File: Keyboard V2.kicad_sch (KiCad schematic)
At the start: 247 parts, among them J0 Conn_01x06_Pin, J1 Conn_01x05_Pin, J2 USB_C_Receptacle_USB2.0_16P, P1 SW_Push, SW1 ESC, SW10 F9, SW11 F10, SW12 F11, SW13 F12, SW14 PrntScrn, SW15 Til, SW16 1, SW17 2, SW18 3, SW19 4, SW2 F1, SW20 5, SW21 6, SW22 7, SW23 8, SW24 RotaryEncoder_Switch, SW25 9, SW26 0, SW27 Min, SW28 Plus, SW29 Bs, SW3 F2, SW30 Del, SW31 Tab, SW32 Q, SW33 W, SW34 E, SW35 R, SW36 T, SW37 Y, SW38 U, SW39 I, SW4 F3, SW40 O, SW41 P, SW42 LBrck, SW43 RBrck, SW44 BSlsh, SW45 Home, SW46 Caps, SW47 A, SW48 S, SW49 D, SW5 F4, SW50 F, SW51 G, SW52 H, SW53 J, SW54 K, SW55 L, SW56 Semi, SW57 Quot, SW58 Enter, SW59 End, SW6 F5, SW60 LShft, SW61 Z, SW62 X, SW63 C, SW64 V, SW65 B, SW66 N, SW67 M, SW68 Comma, SW69 Prd, SW7 F6, SW70 Slash, SW71 RShft, SW72 Up, SW73 LCtrl, SW74 Supr, SW75 Alt, SW76 Space, SW77 RAlt, SW78 Fn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

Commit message: finish esp32-31 version
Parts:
- removed C0: 5uF, symbol Device:C
- removed C109, C120: 1uF, Capacitor_SMD:C_0402_1005Metric, symbol Device:C
- removed C111, C96, C97: 2.2uF, Capacitor_SMD:C_0402_1005Metric, symbol Device:C
- removed C112, C113, C114, C117, C92, C93, C94, C95, C98: 100nF, Capacitor_SMD:C_0402_1005Metric, symbol Device:C
- removed C78, C89: 10uF, Capacitor_SMD:C_0805_2012Metric, symbol Device:C
- removed C88: 100nF, Capacitor_SMD:C_0603_1608Metric, symbol Device:C
- removed C90, C91: 30pF, Capacitor_SMD:C_0402_1005Metric, symbol Device:C
- removed FB1: FerriteBead, Inductor_SMD:L_0603_1608Metric, symbol Device:FerriteBead
- removed FID1, FID2, FID3: Fiducial, Fiducial:Fiducial_1mm_Mask2mm, symbol Mechanical:Fiducial
- removed J1: Conn_01x05_Pin, Connector_PinHeader_2.54mm:PinHeader_1x05_P2.54mm_Horizontal, symbol Connector:Conn_01x05_Pin
- removed R1: 100ohm, Resistor_SMD:R_0603_1608Metric, symbol Device:R
- removed R13: 1k, Resistor_SMD:R_0402_1005Metric, symbol Device:R
- removed R16: 10K, Resistor_SMD:R_0402_1005Metric, symbol Device:R
- removed R19: 1k, Resistor_SMD:R_0603_1608Metric, symbol Device:R
- removed R2: 10K, Resistor_SMD:R_0603_1608Metric, symbol Device:R
- removed U1: MCP1700T-3302E/MAY, DFN-S6_2x2MC_MCH, symbol 2026-08-06_20-43-36:MCP1700T-3302E_MAY
- removed U2: STM32F723IEK6, STM32F723IEK6:IC_STM32F723IEK6, symbol STM32F723IEK6:STM32F723IEK6
- removed Y1: Crystal_GND24, Crystal:Crystal_SMD_Abracon_ABM8G-4Pin_3.2x2.5mm, symbol Device:Crystal_GND24
- added C100, C101, C102: 100nF, Capacitor_SMD:C_0402_1005Metric, symbol Device:C
- added C103: 1uF, Capacitor_SMD:C_0603_1608Metric, symbol Device:C
- added C104: 10uF, Capacitor_SMD:C_0603_1608Metric, symbol Device:C_Small
- added H0, H1, H10, H2, H3, H4, H5, H6, H7, H8, H9: MountingHole, MountingHole:MountingHole_2.2mm_M2, symbol Mechanical:MountingHole
- added J1: Battery Connector, Connector_JST:JST_PH_S2B-PH-K_1x02_P2.00mm_Horizontal, symbol Connector:Conn_01x02_Pin
- added J3: Conn_01x18_Pin, FH34SRJ-18S-0.5SH(50):HRS_FH34SRJ-18S-0.5SH_50_, symbol Connector:Conn_01x18_Pin
- added L0: 470nH, Inductor_SMD:L_0805_2012Metric, symbol Device:L
- added P0: SW_Push, PCM_marbastlib-various:SW_SPST_SKQG_WithStem, symbol Switch:SW_Push
- added R10, R5, R6, R7: 10K, Resistor_SMD:R_0603_1608Metric, symbol Device:R
- added R14: 100k, Resistor_SMD:R_0402_1005Metric, symbol Device:R
- added R17: 4.7k, Resistor_SMD:R_0402_1005Metric, symbol Device:R
- added R4: 890, Resistor_SMD:R_0402_1005Metric, symbol Device:R
- added TH0: Thermistor_NTC, Connector_JST:JST_SH_SM02B-SRSS-TB_1x02-1MP_P1.00mm_Horizontal, symbol Device:Thermistor_NTC
- added U0: MAX17048, MAX17048G:21-0168_T822&plus_3_MXM, symbol PCM_marbastlib-various:MAX17048
- added U1: BQ24075RGT, Package_DFN_QFN:VQFN-16-1EP_3x3mm_P0.5mm_EP1.6x1.6mm, symbol Battery_Management:BQ24075RGT
- added U3: ESP32-S31-WROOM-3, ESP32-S31:ESP32-S31-WROOM-3, symbol ESP32-S31:ESP32-S31
- added U4: TPS62822DLC, Package_SON:Texas_VSON-HR-8_1.5x2mm_P0.5mm, symbol Regulator_Switching:TPS62822DLC
- C105, C106, C116: value 100nF -> 10uF; footprint Capacitor_SMD:C_0402_1005Metric -> Capacitor_SMD:C_0603_1608Metric
- C107, C110: value 100nF -> 100nf
- C108: value 100nF -> 4.7uF; footprint Capacitor_SMD:C_0402_1005Metric -> Capacitor_SMD:C_0603_1608Metric
- C115: value 100nF -> 1uF
- C118: value 10nF -> 10uF; footprint Capacitor_SMD:C_0402_1005Metric -> Capacitor_SMD:C_0603_1608Metric
- C120: renamed from C99; value 100pF -> 10nF
- C121: renamed from C100; value 100pF -> 10nF
- C122: renamed from C101; value 100pF -> 10nF
- C123: renamed from C102; value 100pF -> 10nF
- C124: renamed from C103; value 100pF -> 10nF
- C125: renamed from C104; value 100pF -> 10nF
- J0: value Conn_01x06_Pin -> Fingerprint Sensor; LCSC (none) -> C160392
- J2: LCSC (none) -> C165948
- P1: LCSC (none) -> C49234130
- R0: renamed from R22; value 100R -> 100
- R1: renamed from R20; value 100R -> 100
- R12: value 1k -> 10K; footprint Resistor_SMD:R_0402_1005Metric -> Resistor_SMD:R_0603_1608Metric
- R15: value 10K -> 453k
- R18: value 10K -> 4.7k; footprint Resistor_SMD:R_0603_1608Metric -> Resistor_SMD:R_0402_1005Metric
- R2: renamed from R21; value 100R -> 100
- R20: renamed from R6; value 100R -> 100
- R21: renamed from R7; value 100R -> 100
- R22: renamed from R8; value 100R -> 100
- R23: renamed from R9; value 100R -> 100
- R24: renamed from R10; value 100R -> 100
- R25: renamed from R11; value 100R -> 100
- R3: value 3.00K -> 1.5k; footprint Resistor_SMD:R_0603_1608Metric -> Resistor_SMD:R_0402_1005Metric
- R8: renamed from R17; value 22R -> 22
- R9: renamed from R14; value 22R -> 22
- S0: renamed from S1; now not fitted
- S1: renamed from S2; now not fitted
- S2: renamed from S3; now not fitted
- S3: renamed from S4; now not fitted
- SW0: renamed from SW1; footprint PCM_marbastlib-he:SW_MX_HE_0deg_1u_DFN -> A1395SEHLT-T:SENSOR_A1395SEHLT-T
- SW1: renamed from SW2; footprint PCM_marbastlib-he:SW_MX_HE_0deg_1u_DFN -> A1395SEHLT-T:SENSOR_A1395SEHLT-T
- SW10: renamed from SW11; footprint PCM_marbastlib-he:SW_MX_HE_0deg_1u_DFN -> A1395SEHLT-T:SENSOR_A1395SEHLT-T
- SW11: renamed from SW12; footprint PCM_marbastlib-he:SW_MX_HE_0deg_1u_DFN -> A1395SEHLT-T:SENSOR_A1395SEHLT-T
- SW12: renamed from SW13; footprint PCM_marbastlib-he:SW_MX_HE_0deg_1u_DFN -> A1395SEHLT-T:SENSOR_A1395SEHLT-T
- SW13: renamed from SW14; footprint PCM_marbastlib-he:SW_MX_HE_0deg_1u_DFN -> A1395SEHLT-T:SENSOR_A1395SEHLT-T
- SW14: renamed from SW15; footprint PCM_marbastlib-he:SW_MX_HE_0deg_1u_DFN -> A1395SEHLT-T:SENSOR_A1395SEHLT-T
- SW15: renamed from SW16; footprint PCM_marbastlib-he:SW_MX_HE_0deg_1u_DFN -> A1395SEHLT-T:SENSOR_A1395SEHLT-T
- SW16: renamed from SW17; footprint PCM_marbastlib-he:SW_MX_HE_0deg_1u_DFN -> A1395SEHLT-T:SENSOR_A1395SEHLT-T
- SW17: renamed from SW18; footprint PCM_marbastlib-he:SW_MX_HE_0deg_1u_DFN -> A1395SEHLT-T:SENSOR_A1395SEHLT-T
- SW18: renamed from SW19; footprint PCM_marbastlib-he:SW_MX_HE_0deg_1u_DFN -> A1395SEHLT-T:SENSOR_A1395SEHLT-T
- SW19: renamed from SW20; footprint PCM_marbastlib-he:SW_MX_HE_0deg_1u_DFN -> A1395SEHLT-T:SENSOR_A1395SEHLT-T
- SW2: renamed from SW3; footprint PCM_marbastlib-he:SW_MX_HE_0deg_1u_DFN -> A1395SEHLT-T:SENSOR_A1395SEHLT-T
- SW20: renamed from SW21; footprint PCM_marbastlib-he:SW_MX_HE_0deg_1u_DFN -> A1395SEHLT-T:SENSOR_A1395SEHLT-T
- SW21: renamed from SW22; footprint PCM_marbastlib-he:SW_MX_HE_0deg_1u_DFN -> A1395SEHLT-T:SENSOR_A1395SEHLT-T
- SW22: renamed from SW23; footprint PCM_marbastlib-he:SW_MX_HE_0deg_1u_DFN -> A1395SEHLT-T:SENSOR_A1395SEHLT-T
- SW24: renamed from SW25; footprint PCM_marbastlib-he:SW_MX_HE_0deg_1u_DFN -> A1395SEHLT-T:SENSOR_A1395SEHLT-T
- SW25: renamed from SW26; footprint PCM_marbastlib-he:SW_MX_HE_0deg_1u_DFN -> A1395SEHLT-T:SENSOR_A1395SEHLT-T
- SW26: renamed from SW27; footprint PCM_marbastlib-he:SW_MX_HE_0deg_1u_DFN -> A1395SEHLT-T:SENSOR_A1395SEHLT-T
- SW27: renamed from SW28; footprint PCM_marbastlib-he:SW_MX_HE_0deg_1u_DFN -> A1395SEHLT-T:SENSOR_A1395SEHLT-T
- SW28: renamed from SW29; footprint PCM_marbastlib-he:SW_MX_HE_0deg_1u_DFN -> A1395SEHLT-T:SENSOR_A1395SEHLT-T
- SW29: renamed from SW30; footprint PCM_marbastlib-he:SW_MX_HE_0deg_1u_DFN -> A1395SEHLT-T:SENSOR_A1395SEHLT-T
- SW3: renamed from SW4; footprint PCM_marbastlib-he:SW_MX_HE_0deg_1u_DFN -> A1395SEHLT-T:SENSOR_A1395SEHLT-T
- SW30: renamed from SW31; footprint PCM_marbastlib-he:SW_MX_HE_0deg_1u_DFN -> A1395SEHLT-T:SENSOR_A1395SEHLT-T
- SW31: renamed from SW32; footprint PCM_marbastlib-he:SW_MX_HE_0deg_1u_DFN -> A1395SEHLT-T:SENSOR_A1395SEHLT-T
- SW32: renamed from SW33; footprint PCM_marbastlib-he:SW_MX_HE_0deg_1u_DFN -> A1395SEHLT-T:SENSOR_A1395SEHLT-T
- SW33: renamed from SW34; footprint PCM_marbastlib-he:SW_MX_HE_0deg_1u_DFN -> A1395SEHLT-T:SENSOR_A1395SEHLT-T
- SW34: renamed from SW35; footprint PCM_marbastlib-he:SW_MX_HE_0deg_1u_DFN -> A1395SEHLT-T:SENSOR_A1395SEHLT-T
- SW35: renamed from SW36; footprint PCM_marbastlib-he:SW_MX_HE_0deg_1u_DFN -> A1395SEHLT-T:SENSOR_A1395SEHLT-T
- SW36: renamed from SW37; footprint PCM_marbastlib-he:SW_MX_HE_0deg_1u_DFN -> A1395SEHLT-T:SENSOR_A1395SEHLT-T
- SW37: renamed from SW38; footprint PCM_marbastlib-he:SW_MX_HE_0deg_1u_DFN -> A1395SEHLT-T:SENSOR_A1395SEHLT-T
- SW38: renamed from SW39; footprint PCM_marbastlib-he:SW_MX_HE_0deg_1u_DFN -> A1395SEHLT-T:SENSOR_A1395SEHLT-T
- SW39: renamed from SW40; footprint PCM_marbastlib-he:SW_MX_HE_0deg_1u_DFN -> A1395SEHLT-T:SENSOR_A1395SEHLT-T
- SW4: renamed from SW5; footprint PCM_marbastlib-he:SW_MX_HE_0deg_1u_DFN -> A1395SEHLT-T:SENSOR_A1395SEHLT-T
- SW40: renamed from SW41; footprint PCM_marbastlib-he:SW_MX_HE_0deg_1u_DFN -> A1395SEHLT-T:SENSOR_A1395SEHLT-T
- SW41: renamed from SW42; footprint PCM_marbastlib-he:SW_MX_HE_0deg_1u_DFN -> A1395SEHLT-T:SENSOR_A1395SEHLT-T
- SW42: renamed from SW43; footprint PCM_marbastlib-he:SW_MX_HE_0deg_1u_DFN -> A1395SEHLT-T:SENSOR_A1395SEHLT-T
- SW43: renamed from SW44; footprint PCM_marbastlib-he:SW_MX_HE_0deg_1u_DFN -> A1395SEHLT-T:SENSOR_A1395SEHLT-T
- SW44: renamed from SW45; footprint PCM_marbastlib-he:SW_MX_HE_0deg_1u_DFN -> A1395SEHLT-T:SENSOR_A1395SEHLT-T
- SW45: renamed from SW46; footprint PCM_marbastlib-he:SW_MX_HE_0deg_1u_DFN -> A1395SEHLT-T:SENSOR_A1395SEHLT-T
- SW46: renamed from SW47; footprint PCM_marbastlib-he:SW_MX_HE_0deg_1u_DFN -> A1395SEHLT-T:SENSOR_A1395SEHLT-T
- SW47: renamed from SW48; footprint PCM_marbastlib-he:SW_MX_HE_0deg_1u_DFN -> A1395SEHLT-T:SENSOR_A1395SEHLT-T
- SW48: renamed from SW49; footprint PCM_marbastlib-he:SW_MX_HE_0deg_1u_DFN -> A1395SEHLT-T:SENSOR_A1395SEHLT-T
- SW49: renamed from SW50; footprint PCM_marbastlib-he:SW_MX_HE_0deg_1u_DFN -> A1395SEHLT-T:SENSOR_A1395SEHLT-T
- SW5: renamed from SW6; footprint PCM_marbastlib-he:SW_MX_HE_0deg_1u_DFN -> A1395SEHLT-T:SENSOR_A1395SEHLT-T
- SW50: renamed from SW51; footprint PCM_marbastlib-he:SW_MX_HE_0deg_1u_DFN -> A1395SEHLT-T:SENSOR_A1395SEHLT-T
- SW51: renamed from SW52; footprint PCM_marbastlib-he:SW_MX_HE_0deg_1u_DFN -> A1395SEHLT-T:SENSOR_A1395SEHLT-T
- SW52: renamed from SW53; footprint PCM_marbastlib-he:SW_MX_HE_0deg_1u_DFN -> A1395SEHLT-T:SENSOR_A1395SEHLT-T
- SW53: renamed from SW54; footprint PCM_marbastlib-he:SW_MX_HE_0deg_1u_DFN -> A1395SEHLT-T:SENSOR_A1395SEHLT-T
- SW54: renamed from SW55; footprint PCM_marbastlib-he:SW_MX_HE_0deg_1u_DFN -> A1395SEHLT-T:SENSOR_A1395SEHLT-T
- SW55: renamed from SW56; footprint PCM_marbastlib-he:SW_MX_HE_0deg_1u_DFN -> A1395SEHLT-T:SENSOR_A1395SEHLT-T
- SW56: renamed from SW57; footprint PCM_marbastlib-he:SW_MX_HE_0deg_1u_DFN -> A1395SEHLT-T:SENSOR_A1395SEHLT-T
- SW57: renamed from SW58; footprint PCM_marbastlib-he:SW_MX_HE_0deg_1u_DFN -> A1395SEHLT-T:SENSOR_A1395SEHLT-T
- SW58: renamed from SW59; footprint PCM_marbastlib-he:SW_MX_HE_0deg_1u_DFN -> A1395SEHLT-T:SENSOR_A1395SEHLT-T
- SW59: renamed from SW60; footprint PCM_marbastlib-he:SW_MX_HE_0deg_1u_DFN -> A1395SEHLT-T:SENSOR_A1395SEHLT-T
- SW6: renamed from SW7; footprint PCM_marbastlib-he:SW_MX_HE_0deg_1u_DFN -> A1395SEHLT-T:SENSOR_A1395SEHLT-T
- SW60: renamed from SW61; footprint PCM_marbastlib-he:SW_MX_HE_0deg_1u_DFN -> A1395SEHLT-T:SENSOR_A1395SEHLT-T
- SW61: renamed from SW62; footprint PCM_marbastlib-he:SW_MX_HE_0deg_1u_DFN -> A1395SEHLT-T:SENSOR_A1395SEHLT-T
- SW62: renamed from SW63; footprint PCM_marbastlib-he:SW_MX_HE_0deg_1u_DFN -> A1395SEHLT-T:SENSOR_A1395SEHLT-T
- SW63: renamed from SW64; footprint PCM_marbastlib-he:SW_MX_HE_0deg_1u_DFN -> A1395SEHLT-T:SENSOR_A1395SEHLT-T
- SW64: renamed from SW65; footprint PCM_marbastlib-he:SW_MX_HE_0deg_1u_DFN -> A1395SEHLT-T:SENSOR_A1395SEHLT-T
- SW65: renamed from SW66; footprint PCM_marbastlib-he:SW_MX_HE_0deg_1u_DFN -> A1395SEHLT-T:SENSOR_A1395SEHLT-T
- SW66: renamed from SW67; footprint PCM_marbastlib-he:SW_MX_HE_0deg_1u_DFN -> A1395SEHLT-T:SENSOR_A1395SEHLT-T
- SW67: renamed from SW68; footprint PCM_marbastlib-he:SW_MX_HE_0deg_1u_DFN -> A1395SEHLT-T:SENSOR_A1395SEHLT-T
- SW68: renamed from SW69; footprint PCM_marbastlib-he:SW_MX_HE_0deg_1u_DFN -> A1395SEHLT-T:SENSOR_A1395SEHLT-T
- SW69: renamed from SW70; footprint PCM_marbastlib-he:SW_MX_HE_0deg_1u_DFN -> A1395SEHLT-T:SENSOR_A1395SEHLT-T
- SW7: renamed from SW8; footprint PCM_marbastlib-he:SW_MX_HE_0deg_1u_DFN -> A1395SEHLT-T:SENSOR_A1395SEHLT-T
- SW70: renamed from SW71; footprint PCM_marbastlib-he:SW_MX_HE_0deg_1u_DFN -> A1395SEHLT-T:SENSOR_A1395SEHLT-T
- SW71: renamed from SW72; footprint PCM_marbastlib-he:SW_MX_HE_0deg_1u_DFN -> A1395SEHLT-T:SENSOR_A1395SEHLT-T
- SW72: renamed from SW73; footprint PCM_marbastlib-he:SW_MX_HE_0deg_1u_DFN -> A1395SEHLT-T:SENSOR_A1395SEHLT-T
- SW73: renamed from SW74; footprint PCM_marbastlib-he:SW_MX_HE_0deg_1u_DFN -> A1395SEHLT-T:SENSOR_A1395SEHLT-T
- SW74: renamed from SW75; footprint PCM_marbastlib-he:SW_MX_HE_0deg_1u_DFN -> A1395SEHLT-T:SENSOR_A1395SEHLT-T
- SW75: renamed from SW76; footprint PCM_marbastlib-he:SW_MX_HE_0deg_1u_DFN -> A1395SEHLT-T:SENSOR_A1395SEHLT-T
- SW76: renamed from SW77; footprint PCM_marbastlib-he:SW_MX_HE_0deg_1u_DFN -> A1395SEHLT-T:SENSOR_A1395SEHLT-T
- SW77: renamed from SW78; footprint PCM_marbastlib-he:SW_MX_HE_0deg_1u_DFN -> A1395SEHLT-T:SENSOR_A1395SEHLT-T
- SW78: renamed from SW79; footprint PCM_marbastlib-he:SW_MX_HE_0deg_1u_DFN -> A1395SEHLT-T:SENSOR_A1395SEHLT-T
- SW79: renamed from SW80; footprint PCM_marbastlib-he:SW_MX_HE_0deg_1u_DFN -> A1395SEHLT-T:SENSOR_A1395SEHLT-T
- SW8: renamed from SW9; footprint PCM_marbastlib-he:SW_MX_HE_0deg_1u_DFN -> A1395SEHLT-T:SENSOR_A1395SEHLT-T
- SW80: renamed from SW81; footprint PCM_marbastlib-he:SW_MX_HE_0deg_1u_DFN -> A1395SEHLT-T:SENSOR_A1395SEHLT-T
- SW9: renamed from SW10; footprint PCM_marbastlib-he:SW_MX_HE_0deg_1u_DFN -> A1395SEHLT-T:SENSOR_A1395SEHLT-T
- renumbered C1 to C0, C2 to C1, C11 to C10, C12 to C11, C13 to C12, C14 to C13, C15 to C14, C16 to C15, C17 to C16, C18 to C17, C19 to C18, C20 to C19, C3 to C2, C21 to C20, C22 to C21, C23 to C22, C24 to C23, C25 to C24, C26 to C25, C27 to C26, C28 to C27, C29 to C28, C30 to C29, C4 to C3, C31 to C30, C32 to C31, C33 to C32, C34 to C33, C35 to C34, C36 to C35, C37 to C36, C38 to C37, C39 to C38, C40 to C39, C5 to C4, C41 to C40, C42 to C41, C43 to C42, C44 to C43, C45 to C44, C46 to C45, C47 to C46, C48 to C47, C49 to C48, C50 to C49, C6 to C5, C51 to C50, C52 to C51, C53 to C52, C54 to C53, C55 to C54, C56 to C55, C57 to C56, C58 to C57, C59 to C58, C60 to C59, C7 to C6, C61 to C60, C62 to C61, C63 to C62, C64 to C63, C65 to C64, C66 to C65, C67 to C66, C68 to C67, C69 to C68, C70 to C69, C8 to C7, C71 to C70, C72 to C71, C73 to C72, C74 to C73, C75 to C74, C76 to C75, C77 to C76, C79 to C77, C80 to C78, C81 to C79, C9 to C8, C82 to C80, C83 to C81, C84 to C82, C85 to C83, C86 to C84, C87 to C85, C10 to C9, C121 to C91, C119 to C98, R4 to R13, R5 to R16, SW24 to SW23, U3 to U5
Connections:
- net +3V3: now also AM0.24 (VCC), AM1.24 (VCC), AM2.24 (VCC), AM3.24 (VCC), AM4.24 (VCC), AM5.24 (VCC), C0.2, C1.2, C10.2, C106.2, C107.2, C11.2, C110.2, C118.2, C12.2, C13.2, C14.2, C15.2, C16.2, C17.2, C18.2, C19.2, C2.2, C20.2, C21.2, C22.2, C23.2, C24.2, C25.2, C26.2, C27.2, C28.2, C29.2, C3.2, C30.2, C31.2, C32.2, C33.2, C34.2, C35.2, C36.2, C37.2, C38.2, C39.2, C4.2, C40.2, C41.2, C42.2, C43.2, C44.2, C45.2, C46.2, C47.2, C48.2, C49.2, C5.2, C50.2, C51.2, C52.2, C53.2, C54.2, C55.2, C56.2, C57.2, C58.2, C59.2, C6.2, C60.2, C61.2, C62.2, C63.2, C64.2, C65.2, C66.2, C67.2, C68.2, C69.2, C7.2, C70.2, C71.2, C72.2, C73.2, C74.2, C75.2, C76.2, C77.2, C78.2, C79.2, C8.2, C80.2, C81.2, C82.2, C83.2, C84.2, C85.2, C9.2, R12.2, R15.1, SW0.1 (VCC), SW0.6 (VREF), SW1.1 (VCC), SW1.6 (VREF), SW10.1 (VCC), SW10.6 (VREF), SW11.1 (VCC), SW11.6 (VREF), SW12.1 (VCC), SW12.6 (VREF), SW13.1 (VCC), SW13.6 (VREF), SW14.1 (VCC), SW14.6 (VREF), SW15.1 (VCC), SW15.6 (VREF), SW16.1 (VCC), SW16.6 (VREF), SW17.1 (VCC), SW17.6 (VREF), SW18.1 (VCC), SW18.6 (VREF), SW19.1 (VCC), SW19.6 (VREF), SW2.1 (VCC), SW2.6 (VREF), SW20.1 (VCC), SW20.6 (VREF), SW21.1 (VCC), SW21.6 (VREF), SW22.1 (VCC), SW22.6 (VREF), SW24.1 (VCC), SW24.6 (VREF), SW25.1 (VCC), SW25.6 (VREF), SW26.1 (VCC), SW26.6 (VREF), SW27.1 (VCC), SW27.6 (VREF), SW28.1 (VCC), SW28.6 (VREF), SW29.1 (VCC), SW29.6 (VREF), SW3.1 (VCC), SW3.6 (VREF), SW30.1 (VCC), SW30.6 (VREF), SW31.1 (VCC), SW31.6 (VREF), SW32.1 (VCC), SW32.6 (VREF), SW33.1 (VCC), SW33.6 (VREF), SW34.1 (VCC), SW34.6 (VREF), SW35.1 (VCC), SW35.6 (VREF), SW36.1 (VCC), SW36.6 (VREF), SW37.1 (VCC), SW37.6 (VREF), SW38.1 (VCC), SW38.6 (VREF), SW39.1 (VCC), SW39.6 (VREF), SW4.1 (VCC), SW4.6 (VREF), SW40.1 (VCC), SW40.6 (VREF), SW41.1 (VCC), SW41.6 (VREF), SW42.1 (VCC), SW42.6 (VREF), SW43.1 (VCC), SW43.6 (VREF), SW44.1 (VCC), SW44.6 (VREF), SW45.1 (VCC), SW45.6 (VREF), SW46.1 (VCC), SW46.6 (VREF), SW47.1 (VCC), SW47.6 (VREF), SW48.1 (VCC), SW48.6 (VREF), SW49.1 (VCC), SW49.6 (VREF), SW5.1 (VCC), SW5.6 (VREF), SW50.1 (VCC), SW50.6 (VREF), SW51.1 (VCC), SW51.6 (VREF), SW52.1 (VCC), SW52.6 (VREF), SW53.1 (VCC), SW53.6 (VREF), SW54.1 (VCC), SW54.6 (VREF), SW55.1 (VCC), SW55.6 (VREF), SW56.1 (VCC), SW56.6 (VREF), SW57.1 (VCC), SW57.6 (VREF), SW58.1 (VCC), SW58.6 (VREF), SW59.1 (VCC), SW59.6 (VREF), SW6.1 (VCC), SW6.6 (VREF), SW60.1 (VCC), SW60.6 (VREF), SW61.1 (VCC), SW61.6 (VREF), SW62.1 (VCC), SW62.6 (VREF), SW63.1 (VCC), SW63.6 (VREF), SW64.1 (VCC), SW64.6 (VREF), SW65.1 (VCC), SW65.6 (VREF), SW66.1 (VCC), SW66.6 (VREF), SW67.1 (VCC), SW67.6 (VREF), SW68.1 (VCC), SW68.6 (VREF), SW69.1 (VCC), SW69.6 (VREF), SW7.1 (VCC), SW7.6 (VREF), SW70.1 (VCC), SW70.6 (VREF), SW71.1 (VCC), SW71.6 (VREF), SW72.1 (VCC), SW72.6 (VREF), SW73.1 (VCC), SW73.6 (VREF), SW74.1 (VCC), SW74.6 (VREF), SW75.1 (VCC), SW75.6 (VREF), SW76.1 (VCC), SW76.6 (VREF), SW77.1 (VCC), SW77.6 (VREF), SW78.1 (VCC), SW78.6 (VREF), SW79.1 (VCC), SW79.6 (VREF), SW8.1 (VCC), SW8.6 (VREF), SW80.1 (VCC), SW80.6 (VREF), SW9.1 (VCC), SW9.6 (VREF), J3.18 (Pin_18), L0.2, R10.2, R5.2, R6.2, R7.2, U0.3 (VDD), U3.3 (+3V3), U3.4 (+3V3); no longer C105.2, C106.1, C107.1, C108.1, C110.1, R15.2, R18.2
- net +5V: now also C103.2, U1.13 (IN), U1.5 (EN2)
- net ENC_A: now also C101.1, R6.1, U3.14 (IO8); no longer R12.2
- net ENC_B: now also C102.2, R7.1, U3.15 (IO9)
- net ENC_SW: now also C100.2, R5.1, U3.13 (IO7)
- net GND: now also C106.1, C107.1, C108.1, C110.1, C115.2, C118.1, P1.2, R3.2, C100.1, C101.2, C102.1, C103.1, C104.1, J1.2 (Pin_2), J3.16 (Pin_16), P0.2, R14.2, R4.1, TH0.2, U0.1 (CTG), U0.4 (GND), U0.6 (QSTRT), U0.9 (GND), U1.15 (SYSOFF), U1.17 (VSS), U1.4 (~{CE}), U1.6 (EN1), U1.8 (VSS), U3.1 (GND), U3.2 (GND), U3.26 (GND), U3.47 (GND), U3.48 (GND), U3.72 (GND), U3.73 (GND), U3.74 (GND), U3.75 (GND), U3.76 (GND), U3.77 (GND), U3.78 (GND), U3.79 (GND), U3.80 (GND), U3.81 (GND), U3.82 (GND), U3.83 (GND), U3.84 (GND), U3.85 (GND), U3.86 (GND), U3.87 (GND), U3.88 (GND), U3.89 (GND), U3.90 (GND), U3.92 (GND), U3.93 (GND), U3.94 (GND), U3.95 (GND), U3.96 (GND), U3.97 (GND), U3.98 (GND), U3.99 (GND), U4.3 (AGND), U4.5 (PGND); no longer C106.2, C107.2, C108.2, C110.2, C115.1, C118.2, P1.1, R3.1
- net MUX_0: now also R25.1; no longer R20.1
- net MUX_1: now also R24.1; no longer R21.1
- net MUX_3: now also R22.1; no longer R24.1
- net MUX_4: now also R21.1; no longer R22.1
- net MUX_5: now also R20.1; no longer R25.1
- net SELECT0: now also U3.46 (IO37)
- net SELECT1: now also U3.49 (IO38)
- net SELECT2: now also U3.50 (IO39)
- net SELECT3: now also U3.51 (IO40)
- net at C124.2, R24.2: now also U3.56 (IO46)
- net CARGE_SDA: now reaches R18.1
- net CARGE_SDA: now also U0.8 (SDA); no longer C118.1
- net at C121.2, R21.2: now also U3.53 (IO43)
- net at C123.2, R23.2: now also U3.55 (IO45)
- net at R12.1: now also C115.1, P1.1, U3.5 (EN); no longer R15.1
- net at C120.2, R20.2: now also U3.52 (IO42)
- net at C122.2, R22.2: now also U3.54 (IO44)
- net at R8.2: now also U3.40 (USB_DP)
- net at C125.2, R25.2: now also U3.57 (IO47)
- net at R9.2: now also U3.41 (USB_DM)
- removed net +3V3A: AM0.24 (VCC), AM1.24 (VCC), AM2.24 (VCC), AM3.24 (VCC), AM4.24 (VCC), AM5.24 (VCC), C0.2, C1.2, C10.2, C11.2, C115.2, C12.2, C13.2, C14.2, C15.2, C16.2, C17.2, C18.2, C19.2, C2.2, C20.2, C21.2, C22.2, C23.2, C24.2, C25.2, C26.2, C27.2, C28.2, C29.2, C3.2, C30.2, C31.2, C32.2, C33.2, C34.2, C35.2, C36.2, C37.2, C38.2, C39.2, C4.2, C40.2, C41.2, C42.2, C43.2, C44.2, C45.2, C46.2, C47.2, C48.2, C49.2, C5.2, C50.2, C51.2, C52.2, C53.2, C54.2, C55.2, C56.2, C57.2, C58.2, C59.2, C6.2, C60.2, C61.2, C62.2, C63.2, C64.2, C65.2, C66.2, C67.2, C68.2, C69.2, C7.2, C70.2, C71.2, C72.2, C73.2, C74.2, C75.2, C76.2, C77.2, C78.2, C79.2, C8.2, C80.2, C81.2, C82.2, C83.2, C84.2, C85.2, C9.2, SW0.1 (VCC), SW0.5 (~{SLEEP}), SW0.6 (VREF), SW1.1 (VCC), SW1.5 (~{SLEEP}), SW1.6 (VREF), SW10.1 (VCC), SW10.5 (~{SLEEP}), SW10.6 (VREF), SW11.1 (VCC), SW11.5 (~{SLEEP}), SW11.6 (VREF), SW12.1 (VCC), SW12.5 (~{SLEEP}), SW12.6 (VREF), SW13.1 (VCC), SW13.5 (~{SLEEP}), SW13.6 (VREF), SW14.1 (VCC), SW14.5 (~{SLEEP}), SW14.6 (VREF), SW15.1 (VCC), SW15.5 (~{SLEEP}), SW15.6 (VREF), SW16.1 (VCC), SW16.5 (~{SLEEP}), SW16.6 (VREF), SW17.1 (VCC), SW17.5 (~{SLEEP}), SW17.6 (VREF), SW18.1 (VCC), SW18.5 (~{SLEEP}), SW18.6 (VREF), SW19.1 (VCC), SW19.5 (~{SLEEP}), SW19.6 (VREF), SW2.1 (VCC), SW2.5 (~{SLEEP}), SW2.6 (VREF), SW20.1 (VCC), SW20.5 (~{SLEEP}), SW20.6 (VREF), SW21.1 (VCC), SW21.5 (~{SLEEP}), SW21.6 (VREF), SW22.1 (VCC), SW22.5 (~{SLEEP}), SW22.6 (VREF), SW24.1 (VCC), SW24.5 (~{SLEEP}), SW24.6 (VREF), SW25.1 (VCC), SW25.5 (~{SLEEP}), SW25.6 (VREF), SW26.1 (VCC), SW26.5 (~{SLEEP}), SW26.6 (VREF), SW27.1 (VCC), SW27.5 (~{SLEEP}), SW27.6 (VREF), SW28.1 (VCC), SW28.5 (~{SLEEP}), SW28.6 (VREF), SW29.1 (VCC), SW29.5 (~{SLEEP}), SW29.6 (VREF), SW3.1 (VCC), SW3.5 (~{SLEEP}), SW3.6 (VREF), SW30.1 (VCC), SW30.5 (~{SLEEP}), SW30.6 (VREF), SW31.1 (VCC), SW31.5 (~{SLEEP}), SW31.6 (VREF), SW32.1 (VCC), SW32.5 (~{SLEEP}), SW32.6 (VREF), SW33.1 (VCC), SW33.5 (~{SLEEP}), SW33.6 (VREF), SW34.1 (VCC), SW34.5 (~{SLEEP}), SW34.6 (VREF), SW35.1 (VCC), SW35.5 (~{SLEEP}), SW35.6 (VREF), SW36.1 (VCC), SW36.5 (~{SLEEP}), SW36.6 (VREF), SW37.1 (VCC), SW37.5 (~{SLEEP}), SW37.6 (VREF), SW38.1 (VCC), SW38.5 (~{SLEEP}), SW38.6 (VREF), SW39.1 (VCC), SW39.5 (~{SLEEP}), SW39.6 (VREF), SW4.1 (VCC), SW4.5 (~{SLEEP}), SW4.6 (VREF), SW40.1 (VCC), SW40.5 (~{SLEEP}), SW40.6 (VREF), SW41.1 (VCC), SW41.5 (~{SLEEP}), SW41.6 (VREF), SW42.1 (VCC), SW42.5 (~{SLEEP}), SW42.6 (VREF), SW43.1 (VCC), SW43.5 (~{SLEEP}), SW43.6 (VREF), SW44.1 (VCC), SW44.5 (~{SLEEP}), SW44.6 (VREF), SW45.1 (VCC), SW45.5 (~{SLEEP}), SW45.6 (VREF), SW46.1 (VCC), SW46.5 (~{SLEEP}), SW46.6 (VREF), SW47.1 (VCC), SW47.5 (~{SLEEP}), SW47.6 (VREF), SW48.1 (VCC), SW48.5 (~{SLEEP}), SW48.6 (VREF), SW49.1 (VCC), SW49.5 (~{SLEEP}), SW49.6 (VREF), SW5.1 (VCC), SW5.5 (~{SLEEP}), SW5.6 (VREF), SW50.1 (VCC), SW50.5 (~{SLEEP}), SW50.6 (VREF), SW51.1 (VCC), SW51.5 (~{SLEEP}), SW51.6 (VREF), SW52.1 (VCC), SW52.5 (~{SLEEP}), SW52.6 (VREF), SW53.1 (VCC), SW53.5 (~{SLEEP}), SW53.6 (VREF), SW54.1 (VCC), SW54.5 (~{SLEEP}), SW54.6 (VREF), SW55.1 (VCC), SW55.5 (~{SLEEP}), SW55.6 (VREF), SW56.1 (VCC), SW56.5 (~{SLEEP}), SW56.6 (VREF), SW57.1 (VCC), SW57.5 (~{SLEEP}), SW57.6 (VREF), SW58.1 (VCC), SW58.5 (~{SLEEP}), SW58.6 (VREF), SW59.1 (VCC), SW59.5 (~{SLEEP}), SW59.6 (VREF), SW6.1 (VCC), SW6.5 (~{SLEEP}), SW6.6 (VREF), SW60.1 (VCC), SW60.5 (~{SLEEP}), SW60.6 (VREF), SW61.1 (VCC), SW61.5 (~{SLEEP}), SW61.6 (VREF), SW62.1 (VCC), SW62.5 (~{SLEEP}), SW62.6 (VREF), SW63.1 (VCC), SW63.5 (~{SLEEP}), SW63.6 (VREF), SW64.1 (VCC), SW64.5 (~{SLEEP}), SW64.6 (VREF), SW65.1 (VCC), SW65.5 (~{SLEEP}), SW65.6 (VREF), SW66.1 (VCC), SW66.5 (~{SLEEP}), SW66.6 (VREF), SW67.1 (VCC), SW67.5 (~{SLEEP}), SW67.6 (VREF), SW68.1 (VCC), SW68.5 (~{SLEEP}), SW68.6 (VREF), SW69.1 (VCC), SW69.5 (~{SLEEP}), SW69.6 (VREF), SW7.1 (VCC), SW7.5 (~{SLEEP}), SW7.6 (VREF), SW70.1 (VCC), SW70.5 (~{SLEEP}), SW70.6 (VREF), SW71.1 (VCC), SW71.5 (~{SLEEP}), SW71.6 (VREF), SW72.1 (VCC), SW72.5 (~{SLEEP}), SW72.6 (VREF), SW73.1 (VCC), SW73.5 (~{SLEEP}), SW73.6 (VREF), SW74.1 (VCC), SW74.5 (~{SLEEP}), SW74.6 (VREF), SW75.1 (VCC), SW75.5 (~{SLEEP}), SW75.6 (VREF), SW76.1 (VCC), SW76.5 (~{SLEEP}), SW76.6 (VREF), SW77.1 (VCC), SW77.5 (~{SLEEP}), SW77.6 (VREF), SW78.1 (VCC), SW78.5 (~{SLEEP}), SW78.6 (VREF), SW79.1 (VCC), SW79.5 (~{SLEEP}), SW79.6 (VREF), SW8.1 (VCC), SW8.5 (~{SLEEP}), SW8.6 (VREF), SW80.1 (VCC), SW80.5 (~{SLEEP}), SW80.6 (VREF), SW9.1 (VCC), SW9.5 (~{SLEEP}), SW9.6 (VREF)
- net RXD renamed RXD_FPRINT
- net RXD_FPRINT: now also U3.17 (IO11)
- net TXD renamed TXD_FPRINT
- net TXD_FPRINT: now also U3.16 (IO10)
- net WAKE_UP renamed WAKE_UP_FPRINT
- net WAKE_UP_FPRINT: now also U3.19 (IO13)
- new net: R4.2, U1.16 (ISET)
- new net: C105.2, C108.2, U1.10 (OUT), U1.11 (OUT), U4.1 (EN), U4.7 (VIN)
- new net: R14.1, R15.2, U4.2 (FB)
- new net: L0.1, U4.6 (SW)
- new net: U3.33 (NC), U3.34 (NC), U3.35 (NC), U3.36 (NC), U3.37 (NC), U3.38 (NC), U3.39 (NC), U3.91 (NC)
- new net: R17.2, U3.42 (IO33)
- new net: R18.2, U3.43 (IO34)
- new net: P0.1, R10.1, U3.8 (IO0)
- new net: TH0.1, U1.1 (TS)
- new net: R3.1, U1.12 (ILIM)
- new net BAT+: C104.2, J1.1 (Pin_1), U0.2 (CELL), U1.2 (BAT), U1.3 (BAT)
- new net BRIGHTNESS: J3.17 (Pin_17), U3.25 (IO19)
- new net CARGE_SCL: R17.1, U0.7 (SCL)
- new net DC: J3.12 (Pin_12), U3.32 (SD_CMD)
- new net HALL_PWR_ON: SW0.5 (~{SLEEP}), SW1.5 (~{SLEEP}), SW10.5 (~{SLEEP}), SW11.5 (~{SLEEP}), SW12.5 (~{SLEEP}), SW13.5 (~{SLEEP}), SW14.5 (~{SLEEP}), SW15.5 (~{SLEEP}), SW16.5 (~{SLEEP}), SW17.5 (~{SLEEP}), SW18.5 (~{SLEEP}), SW19.5 (~{SLEEP}), SW2.5 (~{SLEEP}), SW20.5 (~{SLEEP}), SW21.5 (~{SLEEP}), SW22.5 (~{SLEEP}), SW24.5 (~{SLEEP}), SW25.5 (~{SLEEP}), SW26.5 (~{SLEEP}), SW27.5 (~{SLEEP}), SW28.5 (~{SLEEP}), SW29.5 (~{SLEEP}), SW3.5 (~{SLEEP}), SW30.5 (~{SLEEP}), SW31.5 (~{SLEEP}), SW32.5 (~{SLEEP}), SW33.5 (~{SLEEP}), SW34.5 (~{SLEEP}), SW35.5 (~{SLEEP}), SW36.5 (~{SLEEP}), SW37.5 (~{SLEEP}), SW38.5 (~{SLEEP}), SW39.5 (~{SLEEP}), SW4.5 (~{SLEEP}), SW40.5 (~{SLEEP}), SW41.5 (~{SLEEP}), SW42.5 (~{SLEEP}), SW43.5 (~{SLEEP}), SW44.5 (~{SLEEP}), SW45.5 (~{SLEEP}), SW46.5 (~{SLEEP}), SW47.5 (~{SLEEP}), SW48.5 (~{SLEEP}), SW49.5 (~{SLEEP}), SW5.5 (~{SLEEP}), SW50.5 (~{SLEEP}), SW51.5 (~{SLEEP}), SW52.5 (~{SLEEP}), SW53.5 (~{SLEEP}), SW54.5 (~{SLEEP}), SW55.5 (~{SLEEP}), SW56.5 (~{SLEEP}), SW57.5 (~{SLEEP}), SW58.5 (~{SLEEP}), SW59.5 (~{SLEEP}), SW6.5 (~{SLEEP}), SW60.5 (~{SLEEP}), SW61.5 (~{SLEEP}), SW62.5 (~{SLEEP}), SW63.5 (~{SLEEP}), SW64.5 (~{SLEEP}), SW65.5 (~{SLEEP}), SW66.5 (~{SLEEP}), SW67.5 (~{SLEEP}), SW68.5 (~{SLEEP}), SW69.5 (~{SLEEP}), SW7.5 (~{SLEEP}), SW70.5 (~{SLEEP}), SW71.5 (~{SLEEP}), SW72.5 (~{SLEEP}), SW73.5 (~{SLEEP}), SW74.5 (~{SLEEP}), SW75.5 (~{SLEEP}), SW76.5 (~{SLEEP}), SW77.5 (~{SLEEP}), SW78.5 (~{SLEEP}), SW79.5 (~{SLEEP}), SW8.5 (~{SLEEP}), SW80.5 (~{SLEEP}), SW9.5 (~{SLEEP}), U3.18 (IO12)
- new net MISO: J3.13 (Pin_13), U3.29 (SD_D2)
- new net MOSI: J3.14 (Pin_14), U3.28 (SD_D1)
- new net RST: J3.11 (Pin_11), U3.24 (IO18)
- new net SCK: J3.15 (Pin_15), U3.27 (SD_D0)
- new net SDCS: J3.9 (Pin_9), U3.31 (SD_CLK)
- new net TCS: J3.10 (Pin_10), U3.30 (SD_D3)
- no-connect marks 142 -> 63
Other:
- moved on the sheet: C120, C121, C122, C123, C124, C125, C85, C91, C98, J0, J2, R0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

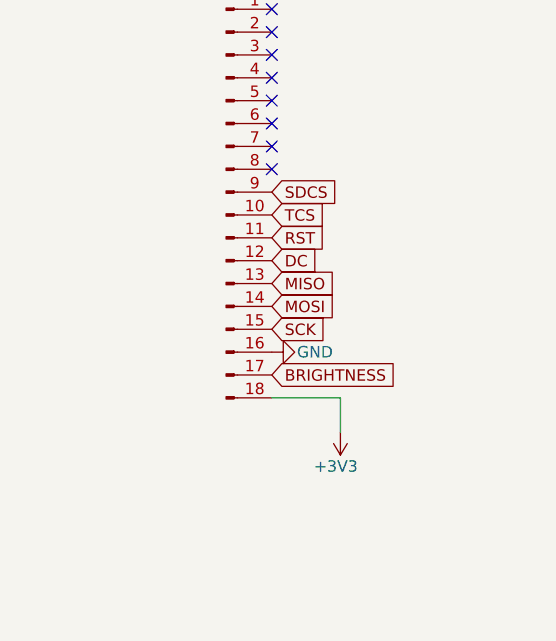
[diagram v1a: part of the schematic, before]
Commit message: add forgotten display passive components
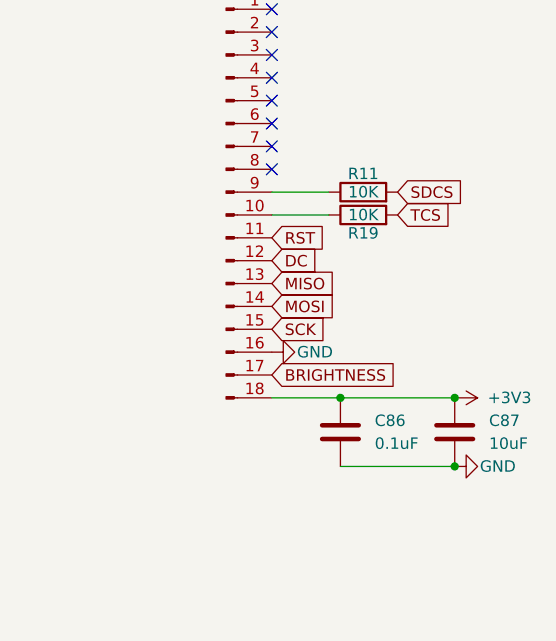
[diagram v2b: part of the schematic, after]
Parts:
- added C86: 0.1uF, Capacitor_SMD:C_0402_1005Metric, symbol Device:C
- added C87: 10uF, Capacitor_SMD:C_0603_1608Metric, symbol Device:C
- added R11, R19: 10K, Resistor_SMD:R_0402_1005Metric, symbol Device:R
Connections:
- net +3V3: now also C86.1, C87.1
- net GND: now also C86.2, C87.2
- net SDCS: now also R11.2; no longer J3.9 (Pin_9)
- net TCS: now also R19.2; no longer J3.10 (Pin_10)
- new net: J3.10 (Pin_10), R19.1
- new net: J3.9 (Pin_9), R11.1
